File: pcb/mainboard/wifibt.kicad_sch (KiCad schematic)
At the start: 10 parts

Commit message: Working on mainboard schematics
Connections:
- net +3V3: no longer C?.1, C?.1, U?.9 (VBAT)
- net UART2_CTS renamed UART1_RTS
- net UART2_RTS renamed UART1_CTS
- net UART2_RXD renamed UART1_RXD
- net UART2_TXD renamed UART1_TXD
- new net +BATT: C?.1, C?.1, U?.9 (VBAT)
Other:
- moved on the sheet: ANT?, C?, R?, U?

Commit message: Mainboard schematics WIP
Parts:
- removed ANT?: PCB_WIFI_ANT, footprints:bt_antenna_1ant_2gnd, symbol symbols:WIFI_ANT_ESP8266
- removed C?: 33pF/50V/5%, Capacitor_SMD:C_0402_1005Metric, symbol Device:C
- removed C? (x2): 100nF, Capacitor_SMD:C_0402_1005Metric, symbol Device:C
- removed C? (x2): 10uF, Capacitor_SMD:C_0603_1608Metric, symbol Device:C
- removed C? (x2): DNP, Capacitor_SMD:C_0402_1005Metric, symbol Device:C
- removed R?: 0R, Resistor_SMD:R_0402_1005Metric, symbol Device:R
- added C901, C902: 18pF, Capacitor_SMD:C_0402_1005Metric, symbol Device:C
- added C903, C906: DNP, Capacitor_SMD:C_0402_1005Metric, symbol Device:C
- added C904, C908: 100nF, Capacitor_SMD:C_0402_1005Metric, symbol Device:C
- added C905, C907, C909: 10uF, Capacitor_SMD:C_0603_1608Metric, symbol Device:C
- added J901: U.FL Connector, Connector_Coaxial:U.FL_Molex_MCRF_73412-0110_Vertical, symbol Connector:Conn_Coaxial
- added L901: 4.7uH, footprints:L_1212, symbol Device:L
- added R901: 22, Resistor_SMD:R_0402_1005Metric, symbol Device:R
- added R902: 0R, Resistor_SMD:R_0402_1005Metric, symbol Device:R
- added Y901: 26MHz, Oscillator:Oscillator_SMD_Abracon_ASE-4Pin_3.2x2.5mm, symbol Device:Crystal_GND24
- gave numbers to parts that had none: 1
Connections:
- net +BATT is gone; now on net +3V3: U901.9 (VBAT)
- net +3V3: now also C904.1, C907.1, C908.1, C909.1
- net GND: now also U901.1 (GND), U901.20 (GND), U901.31 (GND), U901.33 (GND), U901.36 (GND), C901.2, C902.2, C903.1, C904.2, C905.2, C906.1, C907.2, C908.2, C909.2, J901.2 (Ext), Y901.2, Y901.4; no longer U901.11 (XTAL_OUT), U901.2 (WIFI/BT_ANT), U901.23 (VIN_LDO), U901.4 (FM_RX)
- net at U901.10 (XTAL_IN): now also C901.1, Y901.3
- net at U901.21 (VIN_LDO_OUT): now also L901.1
- new net: C902.1, R901.1, Y901.1
- new net: C905.1, L901.2, U901.23 (VIN_LDO)
- new net: C903.2, R902.2, U901.2 (WIFI/BT_ANT)
- new net: C906.2, J901.1 (In), R902.1
- new net: R901.2, U901.11 (XTAL_OUT)

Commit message: Draft motherboard schematics for r0.0 layout
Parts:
- C904, C908: footprint Capacitor_SMD:C_0402_1005Metric -> Capacitor_SMD:C_0201_0603Metric
- L901: footprint footprints:L_1212 -> Inductor_SMD:L_1210_3225Metric
- R902: value 0R -> 0
- U901: footprint footprints:RL-SM02BD(RTL8723BS) -> footprint:RL-SM02BD(RTL8723BS)
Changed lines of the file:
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@@
       (effects (font (size 1.27 1.27)) (justify left))
     )
-    (property "Footprint" "Capacitor_SMD:C_0402_1005Metric" (id 2) (at 214.3252 73.66 0)
+    (property "Footprint" "Capacitor_SMD:C_0201_0603Metric" (id 2) (at 214.3252 73.66 0)
       (effects (font (size 1.27 1.27)) hide)
     )
@@
     (property "Reference" "L901" (id 0) (at 171.45 77.47 90))
     (property "Value" "4.7uH" (id 1) (at 181.61 77.47 90))
-    (property "Footprint" "footprints:L_1212" (id 2) (at 176.53 78.74 0)
+    (property "Footprint" "Inductor_SMD:L_1210_3225Metric" (id 2) (at 176.53 78.74 0)
       (effects (font (size 1.27 1.27)) hide)
     )
@@
       (effects (font (size 1.524 1.524)))
     )
-    (property "Footprint" "footprints:RL-SM02BD(RTL8723BS)" (id 2) (at 152.4 142.24 0)
+    (property "Footprint" "footprint:RL-SM02BD(RTL8723BS)" (id 2) (at 152.4 142.24 0)
       (effects (font (size 1.524 1.524)) hide)
     )
@@
       (effects (font (size 1.27 1.27)) (justify left))
     )
-    (property "Footprint" "Capacitor_SMD:C_0402_1005Metric" (id 2) (at 188.9252 73.66 0)
+    (property "Footprint" "Capacitor_SMD:C_0201_0603Metric" (id 2) (at 188.9252 73.66 0)
       (effects (font (size 1.27 1.27)) hide)
     )
@@
       (effects (font (size 1.27 1.27)) (justify left))
     )
-    (property "Value" "0R" (id 1) (at 182.88 88.9 90)
-      (effects (font (size 1.27 1.27)) (justify left))
-    )
+    (property "Value" "0" (id 1) (at 182.88 88.9 90)
+      (effects (font (size 1.27 1.27)) (justify left))
+    )

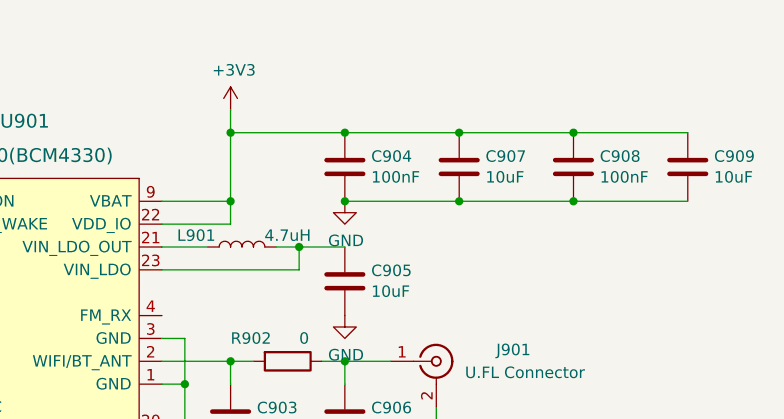
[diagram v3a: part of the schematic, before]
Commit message: Motherboard PCB component initial placement, schematics fixes
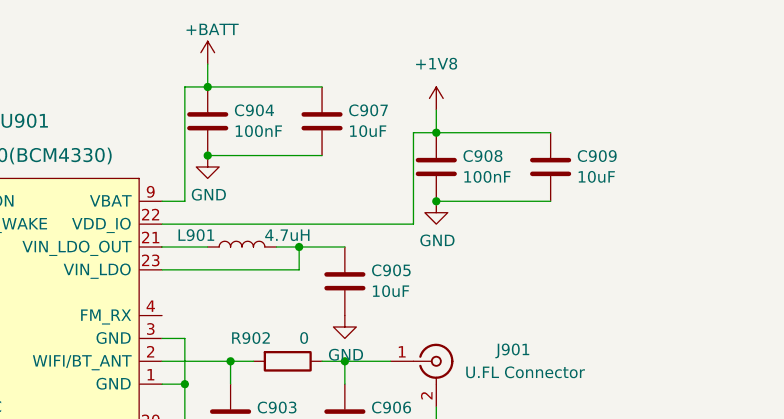
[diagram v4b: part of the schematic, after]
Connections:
- net +3V3 renamed +1V8
- net +1V8: no longer C904.1, C907.1, U901.9 (VBAT)
- new net +BATT: C904.1, C907.1, U901.9 (VBAT)
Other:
- moved on the sheet: C904, C907, C908, C909

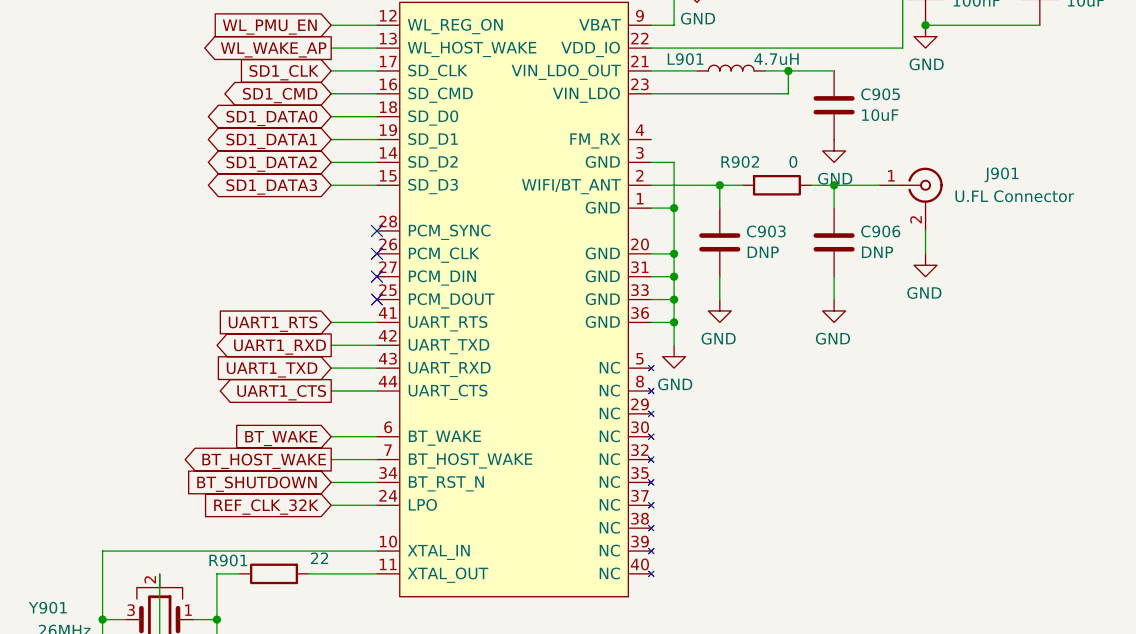
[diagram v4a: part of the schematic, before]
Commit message: Routing mainboard in progress, schematics fixes
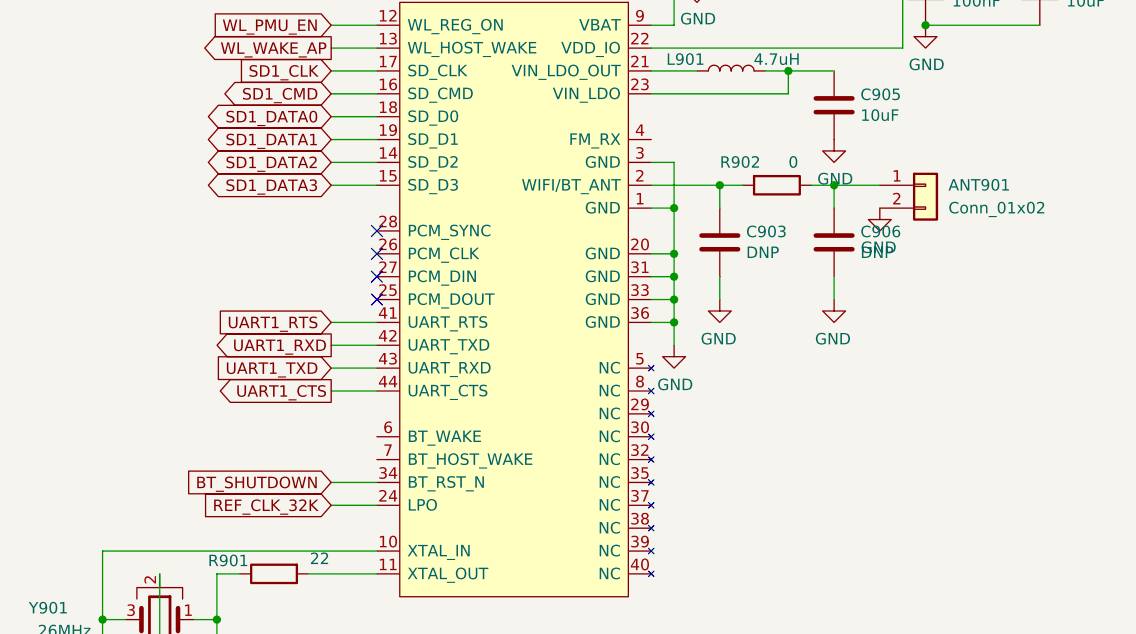
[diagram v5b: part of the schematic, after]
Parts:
- removed J901: U.FL Connector, Connector_Coaxial:U.FL_Molex_MCRF_73412-0110_Vertical, symbol Connector:Conn_Coaxial
- added ANT901: Conn_01x02, RF_Antenna:Texas_SWRA117D_2.4GHz_Right, symbol Connector_Generic:Conn_01x02
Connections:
- net GND: now also ANT901.2 (Pin_2)
- net at C906.2, R902.1: now also ANT901.1 (Pin_1)
- net BT_HOST_WAKE: no longer names the net of U901.7 (BT_HOST_WAKE)
- net BT_WAKE: no longer names the net of U901.6 (BT_WAKE)
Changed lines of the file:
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@@
     (stroke (width 0) (type solid) (color 0 0 0 0))
-  )
-  (wire (pts (xy 132.08 119.38) (xy 137.16 119.38))
-    (stroke (width 0) (type default) (color 0 0 0 0))
   )
   (wire (pts (xy 132.08 109.22) (xy 137.16 109.22))
@@
     (stroke (width 0) (type solid) (color 0 0 0 0))
   )
-  (wire (pts (xy 132.08 121.92) (xy 137.16 121.92))
-    (stroke (width 0) (type default) (color 0 0 0 0))
-  )
   (wire (pts (xy 175.26 101.6) (xy 175.26 104.14))
     (stroke (width 0) (type solid) (color 0 0 0 0))
@@
     (stroke (width 0) (type default) (color 0 0 0 0))
   )
-  (wire (pts (xy 198.12 99.06) (xy 198.12 96.52))
-    (stroke (width 0) (type solid) (color 0 0 0 0))
-  )
   (wire (pts (xy 187.96 93.98) (xy 187.96 91.44))
     (stroke (width 0) (type solid) (color 0 0 0 0))
@@
     )
   )
-  (global_label "BT_WAKE" (shape input) (at 132.08 119.38 180) (fields_autoplaced)
-    (effects (font (size 1.27 1.27)) (justify right))
-    (property "Intersheet References" "${INTERSHEET_REFS}" (id 0) (at 121.5026 119.3006 0)
-      (effects (font (size 1.27 1.27)) (justify right) hide)
-    )
-  )
   (global_label "SD1_DATA2" (shape bidirectional) (at 132.08 88.9 180) (fields_autoplaced)
     (effects (font (size 1.27 1.27)) (justify right))
@@
     (effects (font (size 1.27 1.27)) (justify right))
     (property "Intersheet References" "${INTERSHEET_REFS}" (id 0) (at 119.1954 114.2206 0)
-      (effects (font (size 1.27 1.27)) (justify right) hide)
-    )
-  )
-  (global_label "BT_HOST_WAKE" (shape output) (at 132.08 121.92 180) (fields_autoplaced)
-    (effects (font (size 1.27 1.27)) (justify right))
-    (property "Intersheet References" "${INTERSHEET_REFS}" (id 0) (at 115.6969 121.8406 0)
       (effects (font (size 1.27 1.27)) (justify right) hide)
     )
@@
     (pin "3")
     (pin "4")
+  )
+  (symbol (lib_id "Connector_Generic:Conn_01x02") (at 198.12 91.44 0) (unit 1)
+    (in_bom yes) (on_board yes) (fields_autoplaced)
+    (property "Reference" "ANT901" (id 0) (at 200.66 91.4399 0)
+      (effects (font (size 1.27 1.27)) (justify left))
+    )
+    (property "Value" "Conn_01x02" (id 1) (at 200.66 93.9799 0)
+      (effects (font (size 1.27 1.27)) (justify left))
+    )
+    (property "Footprint" "RF_Antenna:Texas_SWRA117D_2.4GHz_Right" (id 2) (at 198.12 91.44 0)
+      (effects (font (size 1.27 1.27)) hide)
+    )
+    (property "Datasheet" "~" (id 3) (at 198.12 91.44 0)
+      (effects (font (size 1.27 1.27)) hide)
+    )
+    (pin "1")
+    (pin "2")
   )
   (symbol (lib_id "Device:C") (at 210.82 69.85 0) (unit 1)
@@
     )
     (property "Datasheet" "" (id 3) (at 187.96 104.14 0)
-      (effects (font (size 1.27 1.27)) hide)
-    )
-    (pin "1")
-  )
-  (symbol (lib_id "power:GND") (at 198.12 99.06 0) (mirror y) (unit 1)
-    (in_bom yes) (on_board yes)
-    (property "Reference" "#PWR0908" (id 0) (at 198.12 105.41 0)
-      (effects (font (size 1.27 1.27)) hide)
-    )
-    (property "Value" "GND" (id 1) (at 197.993 103.4542 0))
-    (property "Footprint" "" (id 2) (at 198.12 99.06 0)
-      (effects (font (size 1.27 1.27)) hide)
-    )
-    (property "Datasheet" "" (id 3) (at 198.12 99.06 0)
       (effects (font (size 1.27 1.27)) hide)
     )
@@
     (pin "1")
   )
-  (symbol (lib_id "Connector:Conn_Coaxial") (at 198.12 91.44 0) (unit 1)
-    (in_bom yes) (on_board yes)
-    (property "Reference" "J901" (id 0) (at 206.6925 90.17 0))
-    (property "Value" "U.FL Connector" (id 1) (at 207.9625 92.71 0))
-    (property "Footprint" "Connector_Coaxial:U.FL_Molex_MCRF_73412-0110_Vertical" (id 2) (at 198.12 91.44 0)
-      (effects (font (size 1.27 1.27)) hide)
-    )
-    (property "Datasheet" " ~" (id 3) (at 198.12 91.44 0)
-      (effects (font (size 1.27 1.27)) hide)
-    )
-    (pin "1")
-    (pin "2")
-  )
   (symbol (lib_id "power:GND") (at 119.38 149.86 0) (mirror y) (unit 1)
     (in_bom yes) (on_board yes)
@@
       (effects (font (size 1.27 1.27)) hide)
     )
+    (pin "1")
+  )
+  (symbol (lib_id "power:GND") (at 193.04 93.98 0) (mirror y) (unit 1)
+    (in_bom yes) (on_board yes)
+    (property "Reference" "#PWR0156" (id 0) (at 193.04 100.33 0)
+      (effects (font (size 1.27 1.27)) hide)
+    )
+    (property "Value" "GND" (id 1) (at 192.913 98.3742 0))
+    (property "Footprint" "" (id 2) (at 193.04 93.98 0)
+      (effects (font (size 1.27 1.27)) hide)
+    )
+    (property "Datasheet" "" (id 3) (at 193.04 93.98 0)
+      (effects (font (size 1.27 1.27)) hide)
+    )
